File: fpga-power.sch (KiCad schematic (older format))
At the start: 17 parts

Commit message: Add supply remarks
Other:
- note added: "VCCADC max: 2.0V"
- note added: "VCCAUX max: 2.0V"
- note added: "VCCBATT max: 2.0V"
- note added: "VCCBRAM max: 1.1V"
- note added: "VCCINT max: 1.1V"
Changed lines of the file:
@@
 Text Notes 4975 5000 0    50   ~ 0
 Place close to FPGA banks power supply
+Text Notes 7400 2650 1    50   ~ 0
+VCCAUX max: 2.0V
+Text Notes 6825 3350 2    50   ~ 0
+VCCADC max: 2.0V
+Text Notes 6825 3450 2    50   ~ 0
+VCCBATT max: 2.0V
+Text Notes 6825 3550 2    50   ~ 0
+VCCBRAM max: 1.1V
+Text Notes 9750 1925 3    50   ~ 0
+VCCINT max: 1.1V
 $EndSCHEMATC

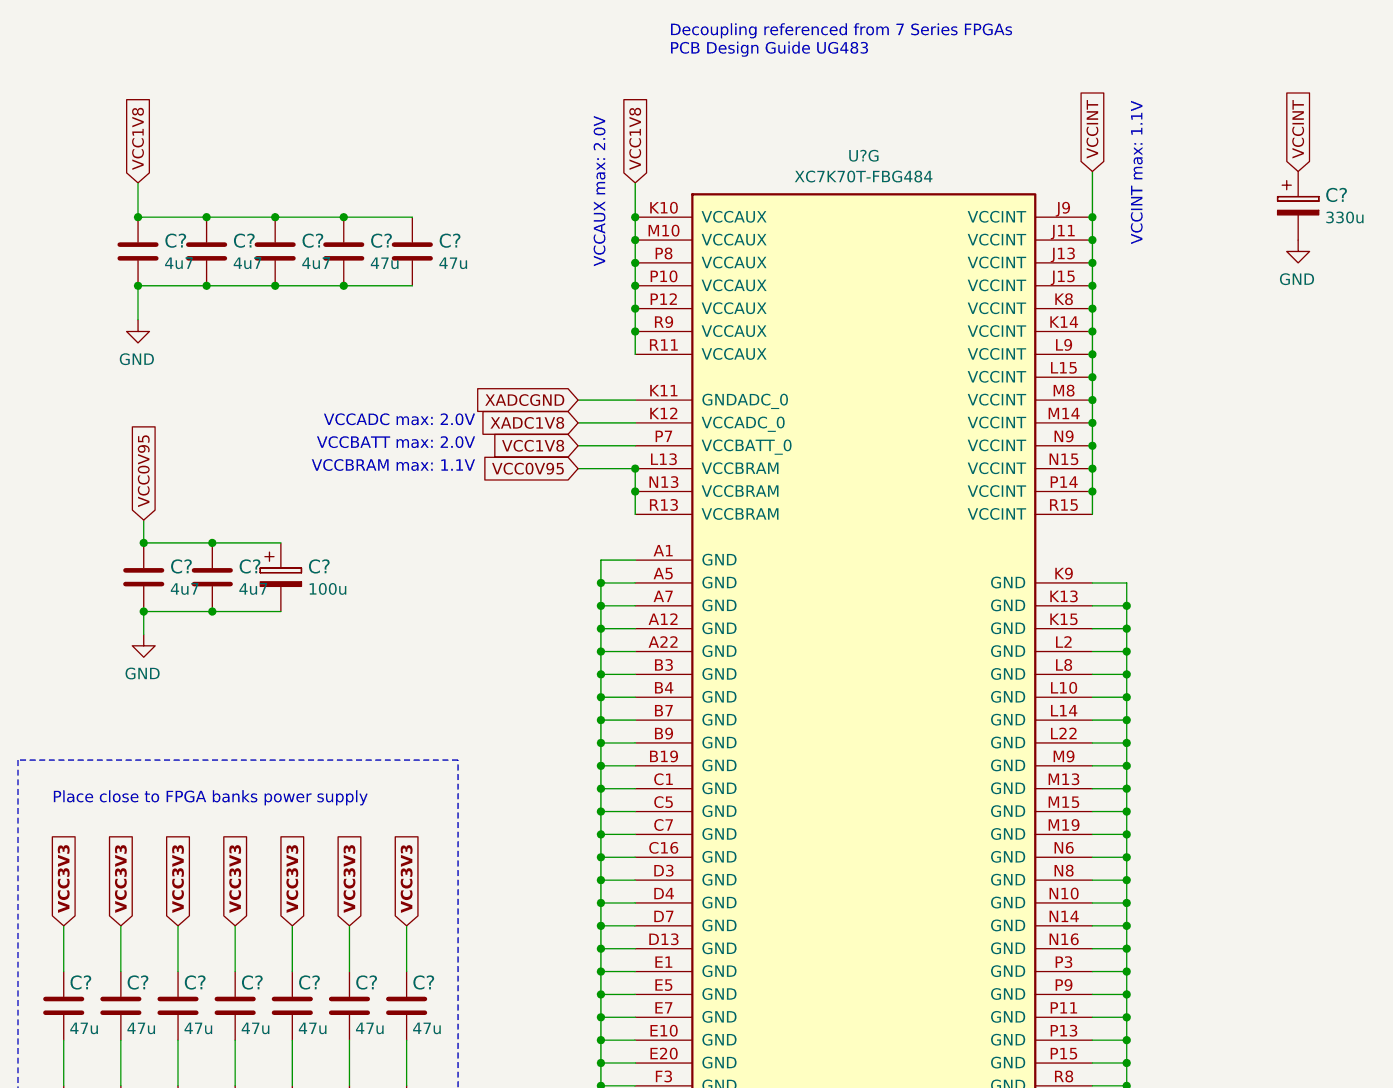
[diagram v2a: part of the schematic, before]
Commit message: Update supply related circuits
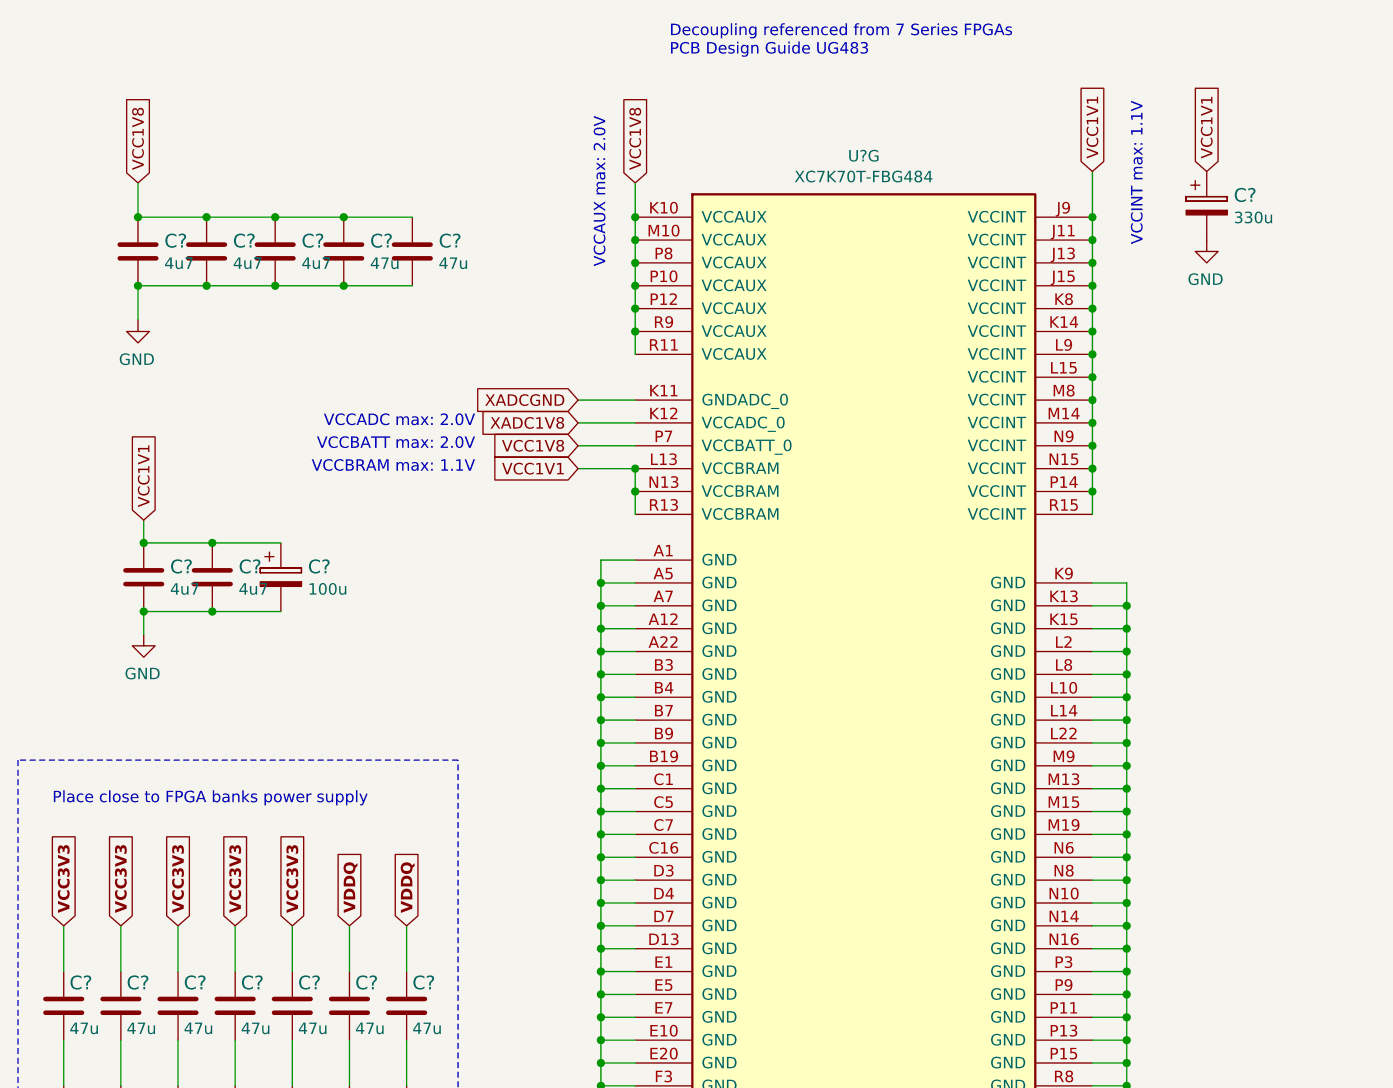
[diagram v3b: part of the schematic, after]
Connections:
- net VCCINT is gone; now on net VCC1V1: C?.1, U?.J11 (VCCINT), U?.J13 (VCCINT), U?.J15 (VCCINT), U?.J9 (VCCINT), U?.K14 (VCCINT), U?.K8 (VCCINT), U?.L15 (VCCINT), U?.L9 (VCCINT), U?.M14 (VCCINT), U?.M8 (VCCINT), U?.N15 (VCCINT), U?.N9 (VCCINT), U?.P14 (VCCINT), U?.R15 (VCCINT)
- net VCC3V3: no longer C?.1, C?.1
- net VCC0V95 renamed VCC1V1
- new net VDDQ: C?.1, C?.1
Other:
- moved on the sheet: C?
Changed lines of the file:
@@
 Connection ~ 7525 3525
 Text GLabel 7275 3525 0    50   Input ~ 0
-VCC0V95
+VCC1V1
 Connection ~ 9525 2525
 Wire Wire Line
@@
 	-1   0    0    -1
 $EndComp
-Text GLabel 5375 3750 1    50   Input ~ 0
-VCC0V95
 $Comp
 L lpddr4-test-board:C_330u_KEMET_D C?
 U 1 1 653DADFB
-P 10425 2325
-F 0 "C?" H 10543 2320 60  0000 L CNN
-F 1 "C_330u_KEMET_D" H 10425 2175 60  0001 C CNN
-F 2 "lpddr4-test-board-footprints:KEMET_D" H 10625 2525 60  0001 L CNN
-F 3 "" H 10425 2325 50  0001 C CNN
-F 4 "KEMET" H 10625 2725 60  0001 L CNN "Manufacturer"
-F 5 "T520D337M006ATE045" H 10625 2625 60  0001 L CNN "MPN"
-F 6 "330u" H 10543 2222 50  0000 L CNN "Val"
-	1    10425 2325
+P 10025 2325
+F 0 "C?" H 10143 2320 60  0000 L CNN
+F 1 "C_330u_KEMET_D" H 10025 2175 60  0001 C CNN
+F 2 "lpddr4-test-board-footprints:KEMET_D" H 10225 2525 60  0001 L CNN
+F 3 "" H 10025 2325 50  0001 C CNN
+F 4 "KEMET" H 10225 2725 60  0001 L CNN "Manufacturer"
+F 5 "T520D337M006ATE045" H 10225 2625 60  0001 L CNN "MPN"
+F 6 "330u" H 10143 2222 50  0000 L CNN "Val"
+	1    10025 2325
 	1    0    0    -1
 $EndComp
@@
 Connection ~ 9525 3125
 Connection ~ 9525 3225
-Text GLabel 9525 2225 1    50   Input ~ 0
-VCCINT
 Wire Wire Line
 	9525 2225 9525 2425
@@
 Wire Wire Line
 	9525 2425 9525 2525
-Text GLabel 10425 2225 1    50   Input ~ 0
-VCCINT
 $Comp
 L lpddr4-test-board:GND #PWR?
 U 1 1 6545DAEF
-P 10425 2525
-F 0 "#PWR?" H 10425 2275 50  0001 C CNN
-F 1 "GND" H 10430 2352 50  0000 C CNN
-F 2 "" H 10425 2525 50  0001 C CNN
-F 3 "" H 10425 2525 50  0001 C CNN
-	1    10425 2525
+P 10025 2525
+F 0 "#PWR?" H 10025 2275 50  0001 C CNN
+F 1 "GND" H 10030 2352 50  0000 C CNN
+F 2 "" H 10025 2525 50  0001 C CNN
+F 3 "" H 10025 2525 50  0001 C CNN
+	1    10025 2525
 	-1   0    0    -1
 $EndComp
@@
 VCC3V3
 Text GLabel 6275 5525 1    50   Input ~ 10
-VCC3V3
+VDDQ
 Text GLabel 6525 5525 1    50   Input ~ 10
-VCC3V3
+VDDQ
 Wire Notes Line
 	4825 4800 4825 6525
@@
 Text Notes 9750 1925 3    50   ~ 0
 VCCINT max: 1.1V
+Text GLabel 9525 2225 1    50   Input ~ 0
+VCC1V1
+Text GLabel 10025 2225 1    50   Input ~ 0
+VCC1V1
+Text GLabel 5375 3750 1    50   Input ~ 0
+VCC1V1
 $EndSCHEMATC
